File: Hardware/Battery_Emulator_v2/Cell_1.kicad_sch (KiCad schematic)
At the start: 28 parts, among them Q1 IRFB7545PBF, SW1 Jumper, SW2 Jumper, U1 MCP4651T-103E_ST, U2 ISO1640BDR, U7 LM317_TO-220, U8 MCP6001UT-I/OT, U9 KA78M05_TO252

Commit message: Modified the v2 pcb
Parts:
- removed RV? (x2): R_POT, Connector_PinHeader_2.54mm:PinHeader_1x03_P2.54mm_Vertical, symbol Device:R_POT
- removed SW1, SW2: Jumper, Jumper:SolderJumper-3_P1.3mm_Open_Pad1.0x1.5mm, symbol Switch:SW_SPDT
- R?: value 390k -> 780k
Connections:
- net at U8.3 (+): now also U1.9 (P0W)
- net at C?.1, U7.1 (ADJ): now also U1.6 (P1W)

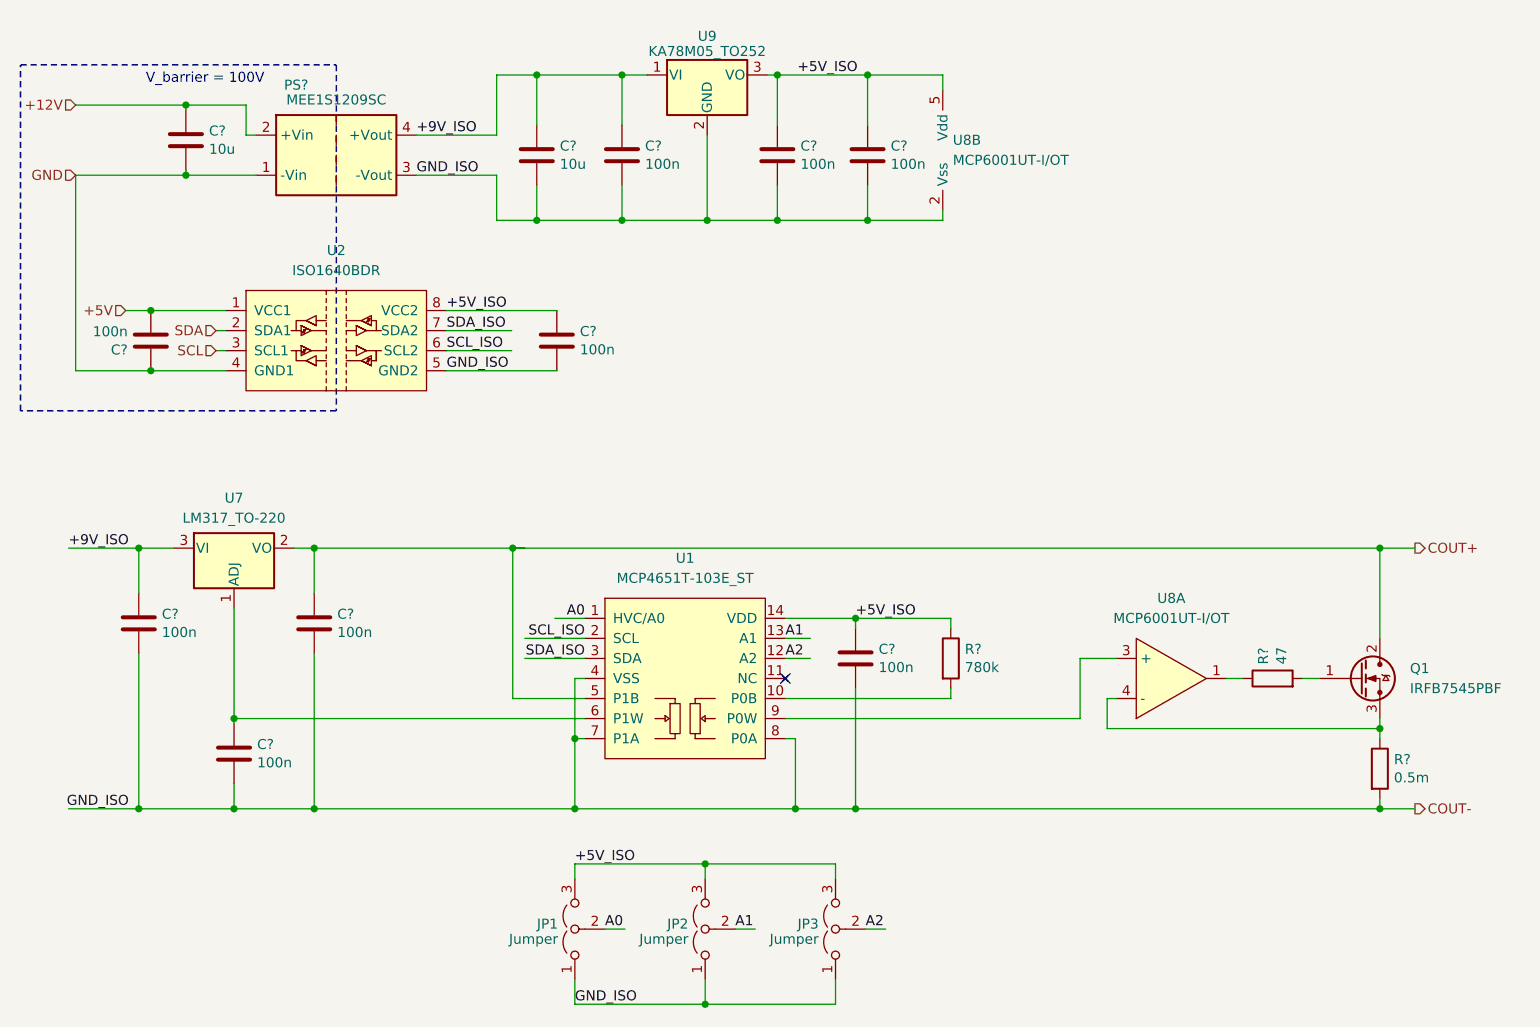
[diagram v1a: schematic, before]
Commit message: Hardware Update
V2 with four cells with the same layout
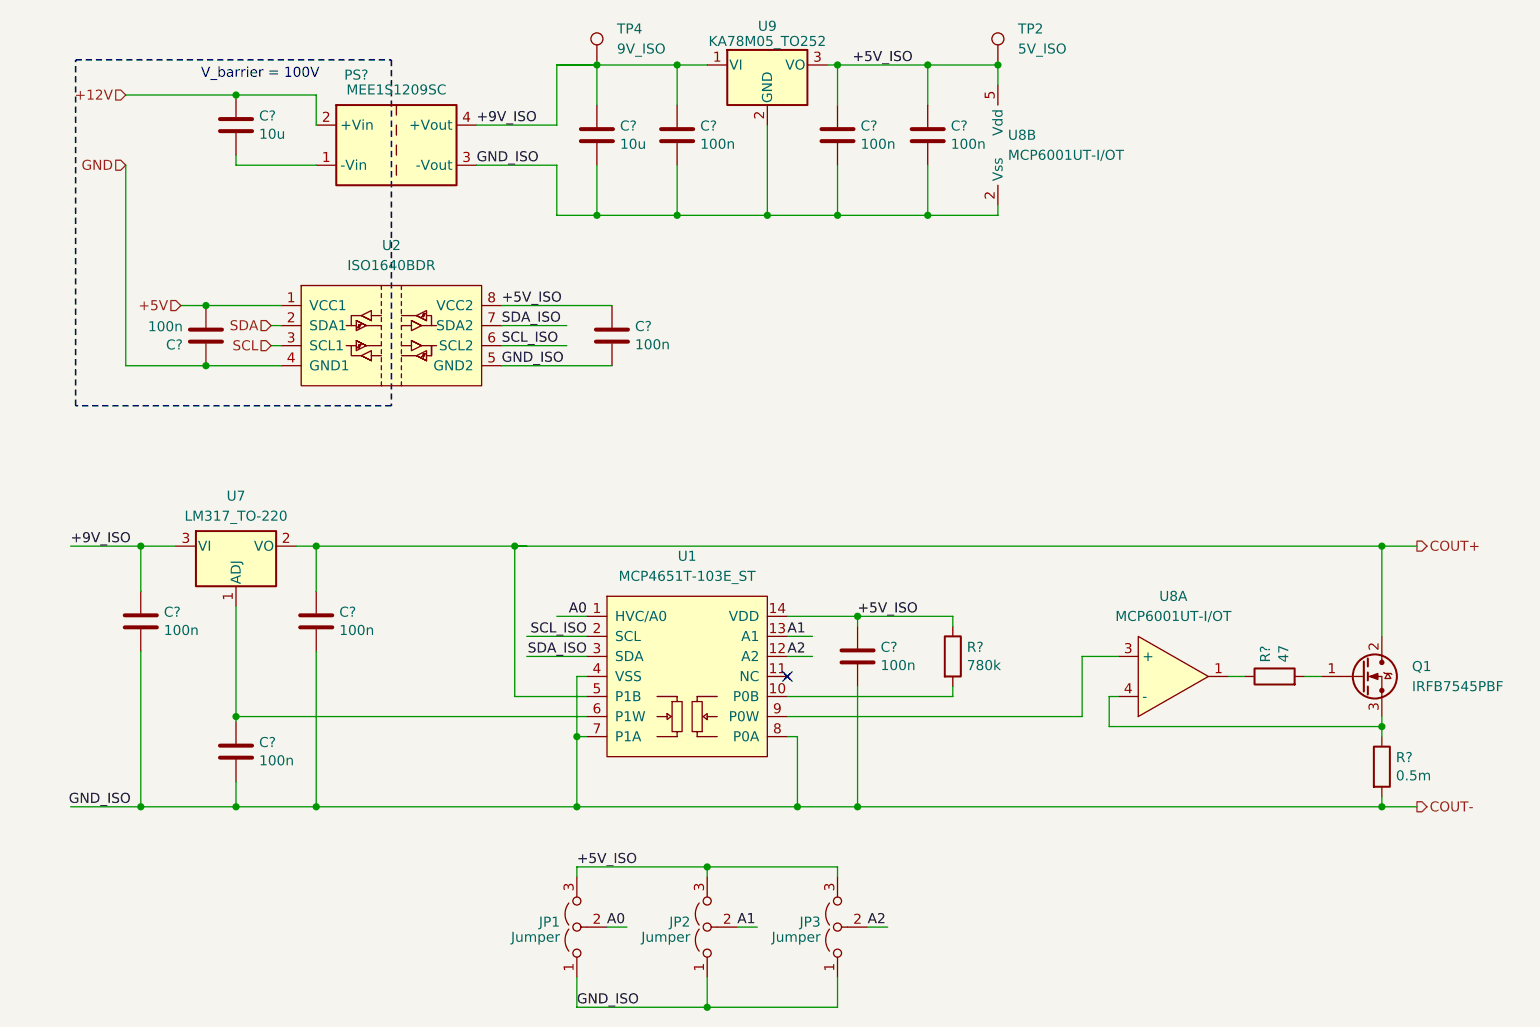
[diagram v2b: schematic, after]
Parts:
- added TP2: 5V_ISO, TestPoint:TestPoint_Pad_D2.5mm, symbol Connector:TestPoint
- added TP4: 9V_ISO, TestPoint:TestPoint_Pad_D2.5mm, symbol Connector:TestPoint
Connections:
- net +5V_ISO: now also TP2.1
- net +9V_ISO: now also TP4.1
- net GND: no longer C?.2, PS?.1 (-Vin)
- new net: C?.2, PS?.1 (-Vin)
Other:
- moved on the sheet: C?, PS?, U2, U8B, U9
